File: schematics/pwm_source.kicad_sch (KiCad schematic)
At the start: 10 parts, among them U4 LM358_DFN, U5 TL331, U6 MCP4725xxx-xCH

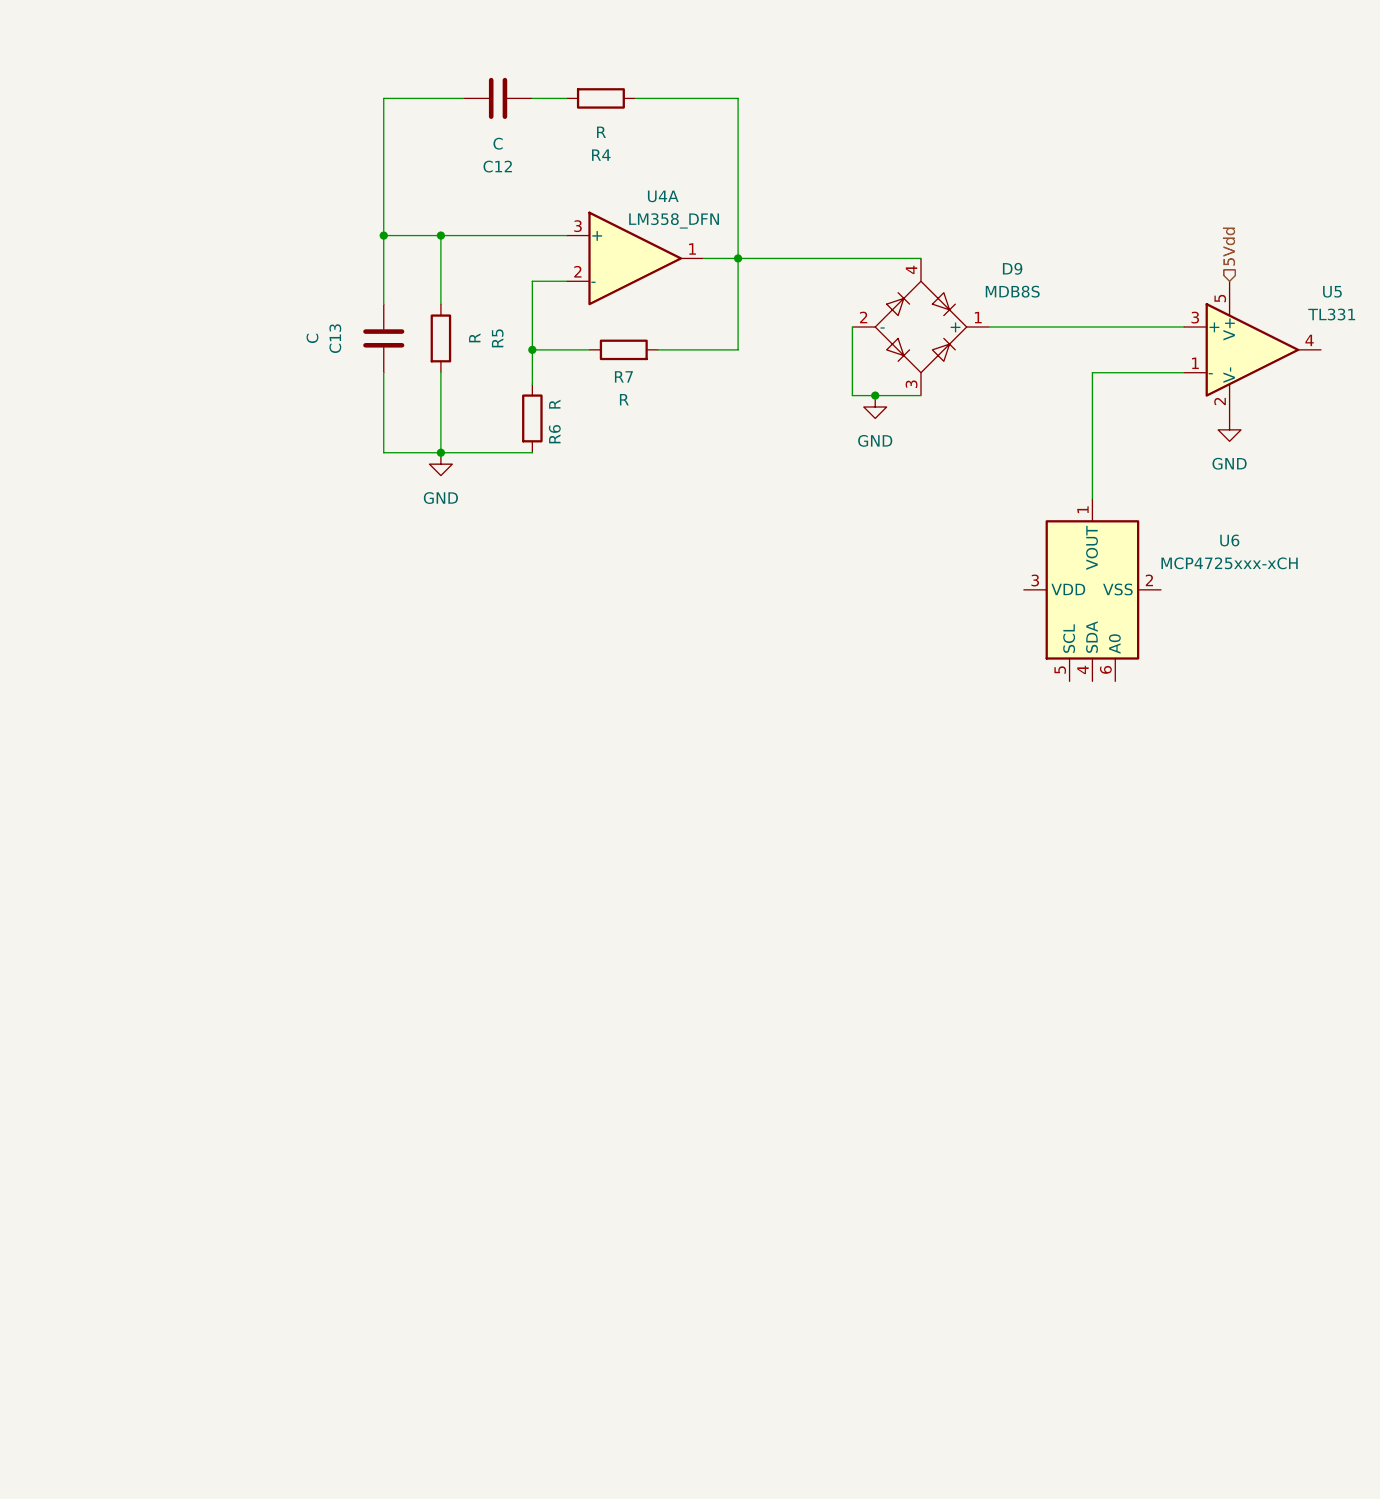
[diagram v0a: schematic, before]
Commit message: worked on oscillator buffering and rectifying
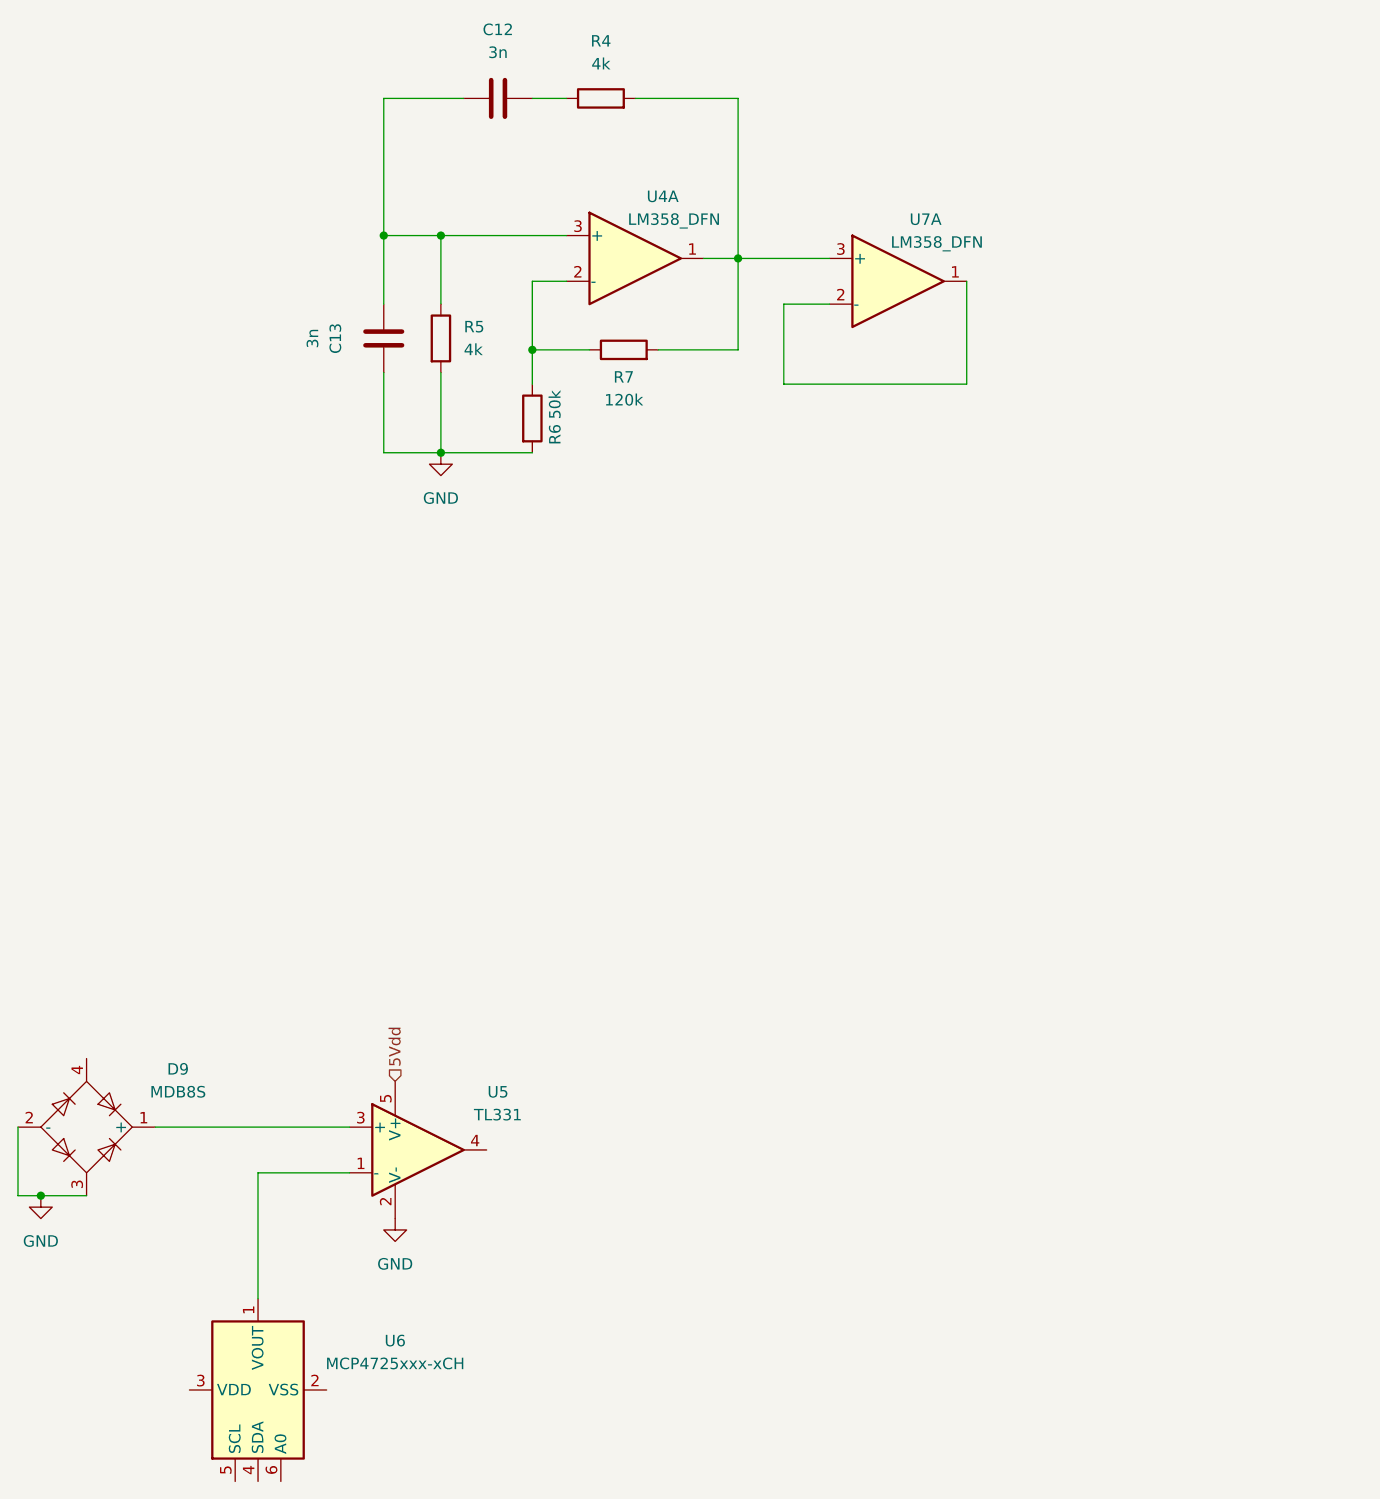
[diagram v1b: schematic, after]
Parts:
- added U7: LM358_DFN, Package_DFN_QFN:DFN-8-1EP_2x2mm_P0.5mm_EP1.05x1.75mm, symbol Amplifier_Operational:LM358_DFN
- C12, C13: value C -> 3n
- R4, R5: value R -> 4k
- R6: value R -> 50k
- R7: value R -> 120k
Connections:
- net at R7.2, U4.1: now also R4.2, U7.3 (+); no longer D9.4, R4.1
- net at C12.1: now also R4.1; no longer R4.2
- new net: U7.1, U7.2 (-)
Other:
- moved on the sheet: D9, R4, U5, U6
